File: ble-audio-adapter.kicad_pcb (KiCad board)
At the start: 2 copper layers, 23 parts, among them P1 AUDIO_JACK_CONN, P2 PWR_SW_CONN, P3 PAIR_BTN_CONN, P4 PLAY/PAUSE_BTN, P5 VOL_UP_BTN, P6 VOL_DOWN_BTN

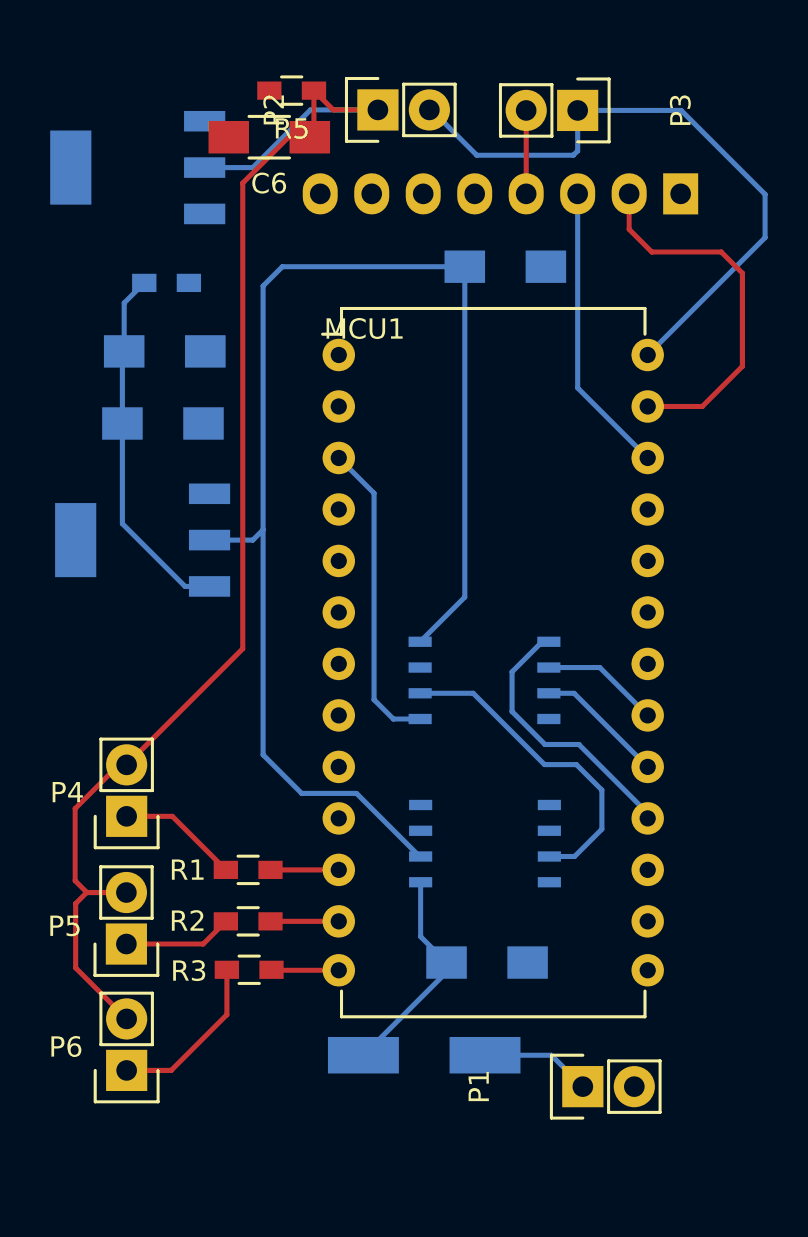
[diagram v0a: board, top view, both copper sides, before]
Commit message: Updated reference positioning
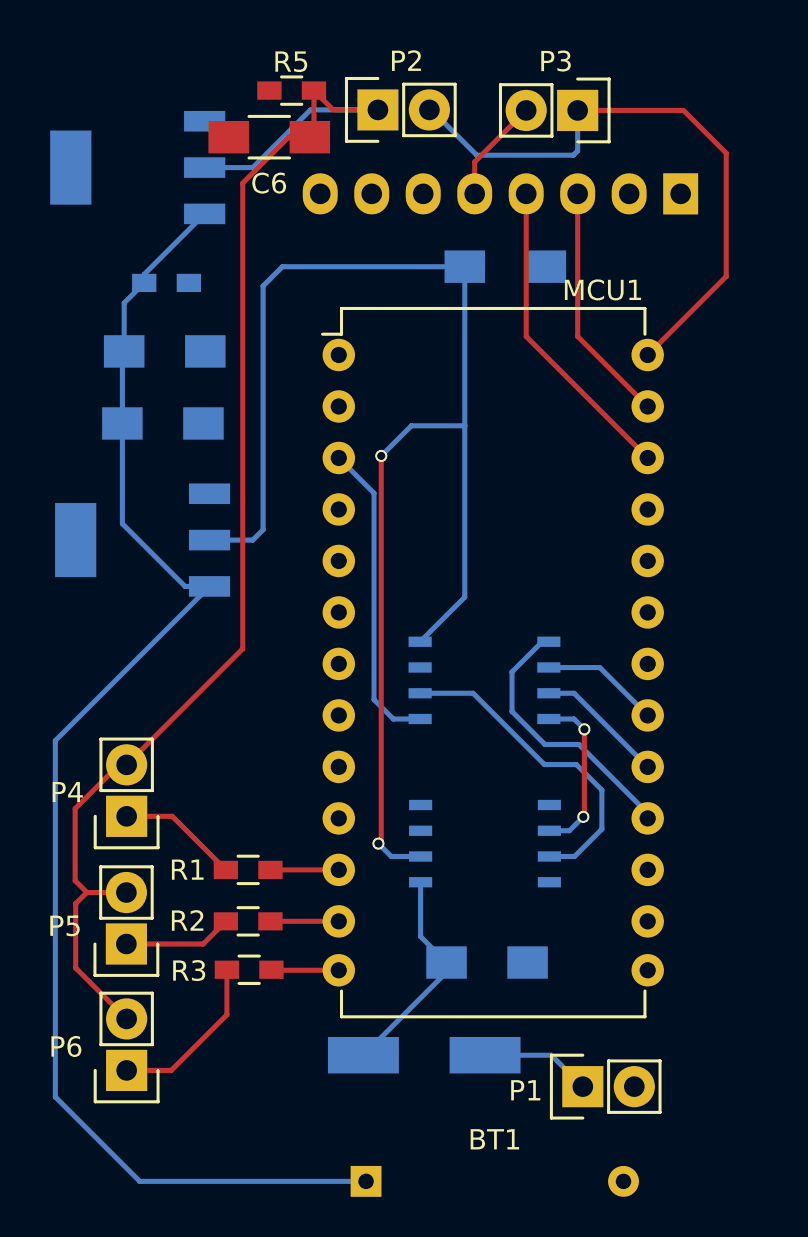
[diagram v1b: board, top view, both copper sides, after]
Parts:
- added BT1: 9V, component_footprints:Battery_Connector, F.Cu at (99.1, 127.1)
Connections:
- BLE1 pad 1: GNDREF -> Net-(BLE1-Pad1)
- BLE1 pad 2: Net-(BLE1-Pad2) -> GNDREF
- BLE1 pad 3: /UART -> Net-(BLE1-Pad3)
- BLE1 pad 4: Net-(BLE1-Pad4) -> /UART
- BLE1 pad 6: GNDREF -> Net-(BLE1-Pad6)
- BLE1 pad 7: Net-(BLE1-Pad7) -> GNDREF
- BLE1 pad 8: (no net) -> Net-(BLE1-Pad8)
- MCU1 pad 25: Net-(BLE1-Pad2) -> Net-(BLE1-Pad3)
- P3 pad 2: Net-(BLE1-Pad4) -> Net-(BLE1-Pad5)
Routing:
- net Net-(BT1-Pad1): track 17.9 -> 67.9 mm
- net Net-(BLE1-Pad2): track 18.3 -> 0.00 mm
- net Net-(BLE1-Pad3): track 0.00 -> 11.9 mm
- net GNDREF: track 0.00 -> 8.26 mm, vias 0 -> 2
- net /5V: track 65.6 -> 71.0 mm, vias 0 -> 2
- net Net-(BLE1-Pad5): track 0.00 -> 5.17 mm
- net Net-(BLE1-Pad4): track 4.11 -> 0.00 mm
- net Net-(MCU1-Pad26): track 31.6 -> 30.1 mm
- net /UART: track 14.5 -> 15.5 mm
